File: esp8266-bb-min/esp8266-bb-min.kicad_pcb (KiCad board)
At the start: 2 copper layers, 31.8 x 39.4 mm, 25 parts, among them J1 Conn_01x02_Male, J2 Conn_01x04_Male, J3 Conn_01x04_Male, J4 Conn_01x06_Male, J5 Conn_01x04_Male, J6 Conn_01x04_Male, J7 Conn_01x02_Male, U1 LP38693MP-3.3, U2 ESP-12F

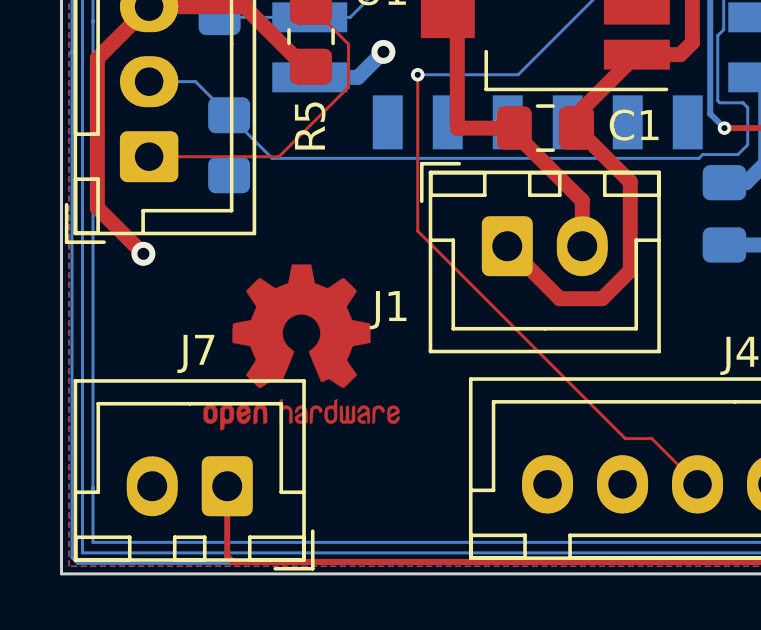
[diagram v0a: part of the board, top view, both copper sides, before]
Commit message: pcb: corrected placement of ohw symbol
Signed-off-by: Dominik Laton <dominik.laton@web.de>
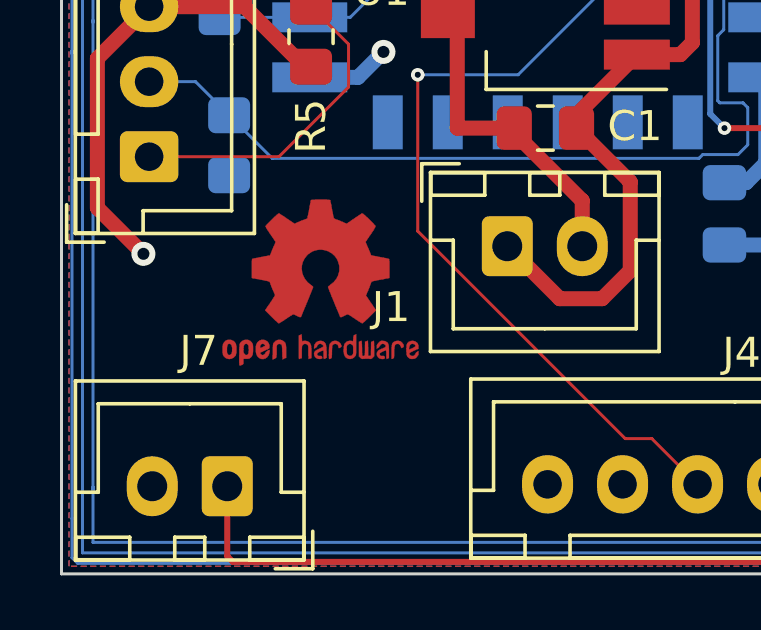
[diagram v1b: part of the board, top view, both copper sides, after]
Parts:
- moved REF** 2.25 mm to (106.3, 101.2)

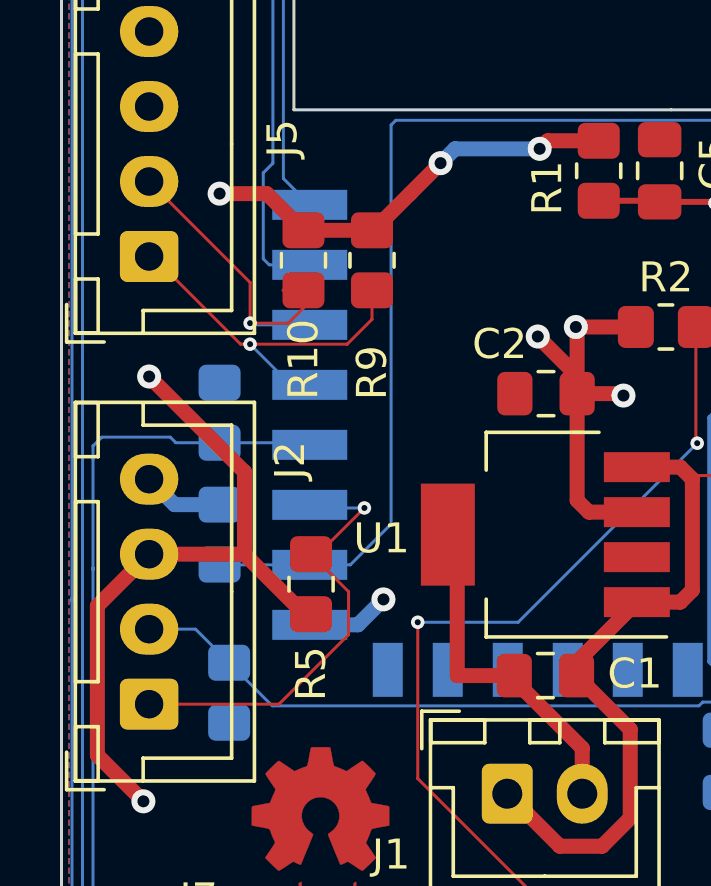
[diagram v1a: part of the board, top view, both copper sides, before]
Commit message: pcb: corrected SCL/SDA pinout
Signed-off-by: Dominik Laton <dominik.laton@web.de>
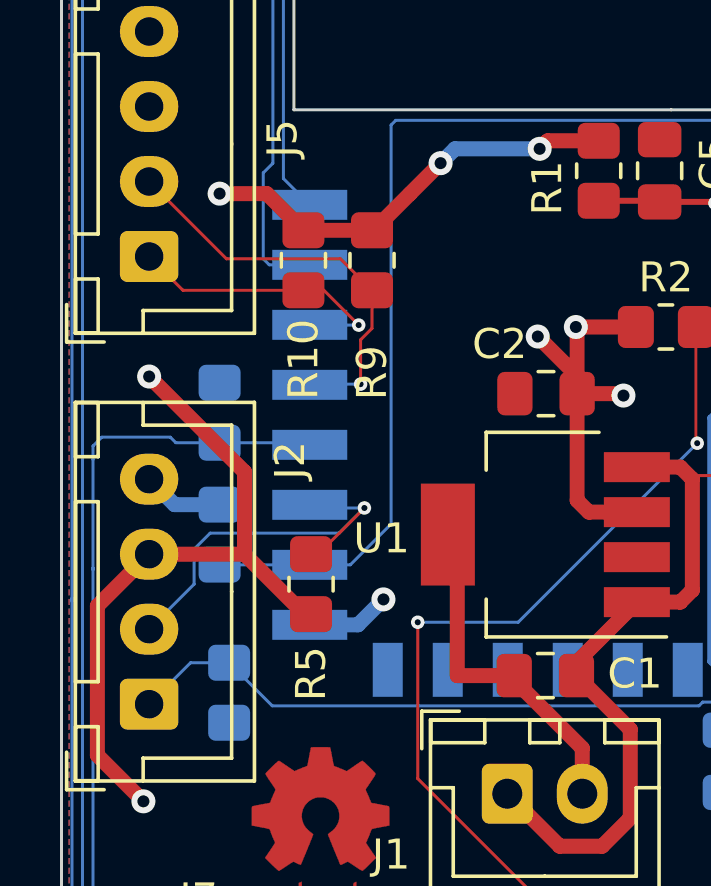
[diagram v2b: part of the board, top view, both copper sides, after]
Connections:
- J2 pad 1: /ESP_GPIO2 -> /ESP_GPIO14
- J2 pad 2: /ESP_GPIO14 -> /ESP_GPIO2
- J5 pad 1: /ESP_GPIO4 -> /ESP_GPIO5
- J5 pad 2: /ESP_GPIO5 -> /ESP_GPIO4
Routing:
- net /ESP_GPIO4: track 12.5 -> 14.6 mm
- net /ESP_GPIO5: track 11.6 -> 10.3 mm
- net /ESP_GPIO2: track 15.5 -> 14.2 mm
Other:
- board text added: "IO14 (SCL)"
- board text added: "IO2 (SDA)"
- board text added: "IO4 (SDA)"
- board text added: "IO5 (SCL)"
- board text removed: "IO14"
- board text removed: "IO2"
- board text removed: "IO4"
- board text removed: "IO5"
